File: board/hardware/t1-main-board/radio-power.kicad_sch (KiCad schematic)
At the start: 25 parts, among them U5101 SN74AXC1T45DCKR, U5102 TPS22919DCKR, U5103 TPS62826DMQR

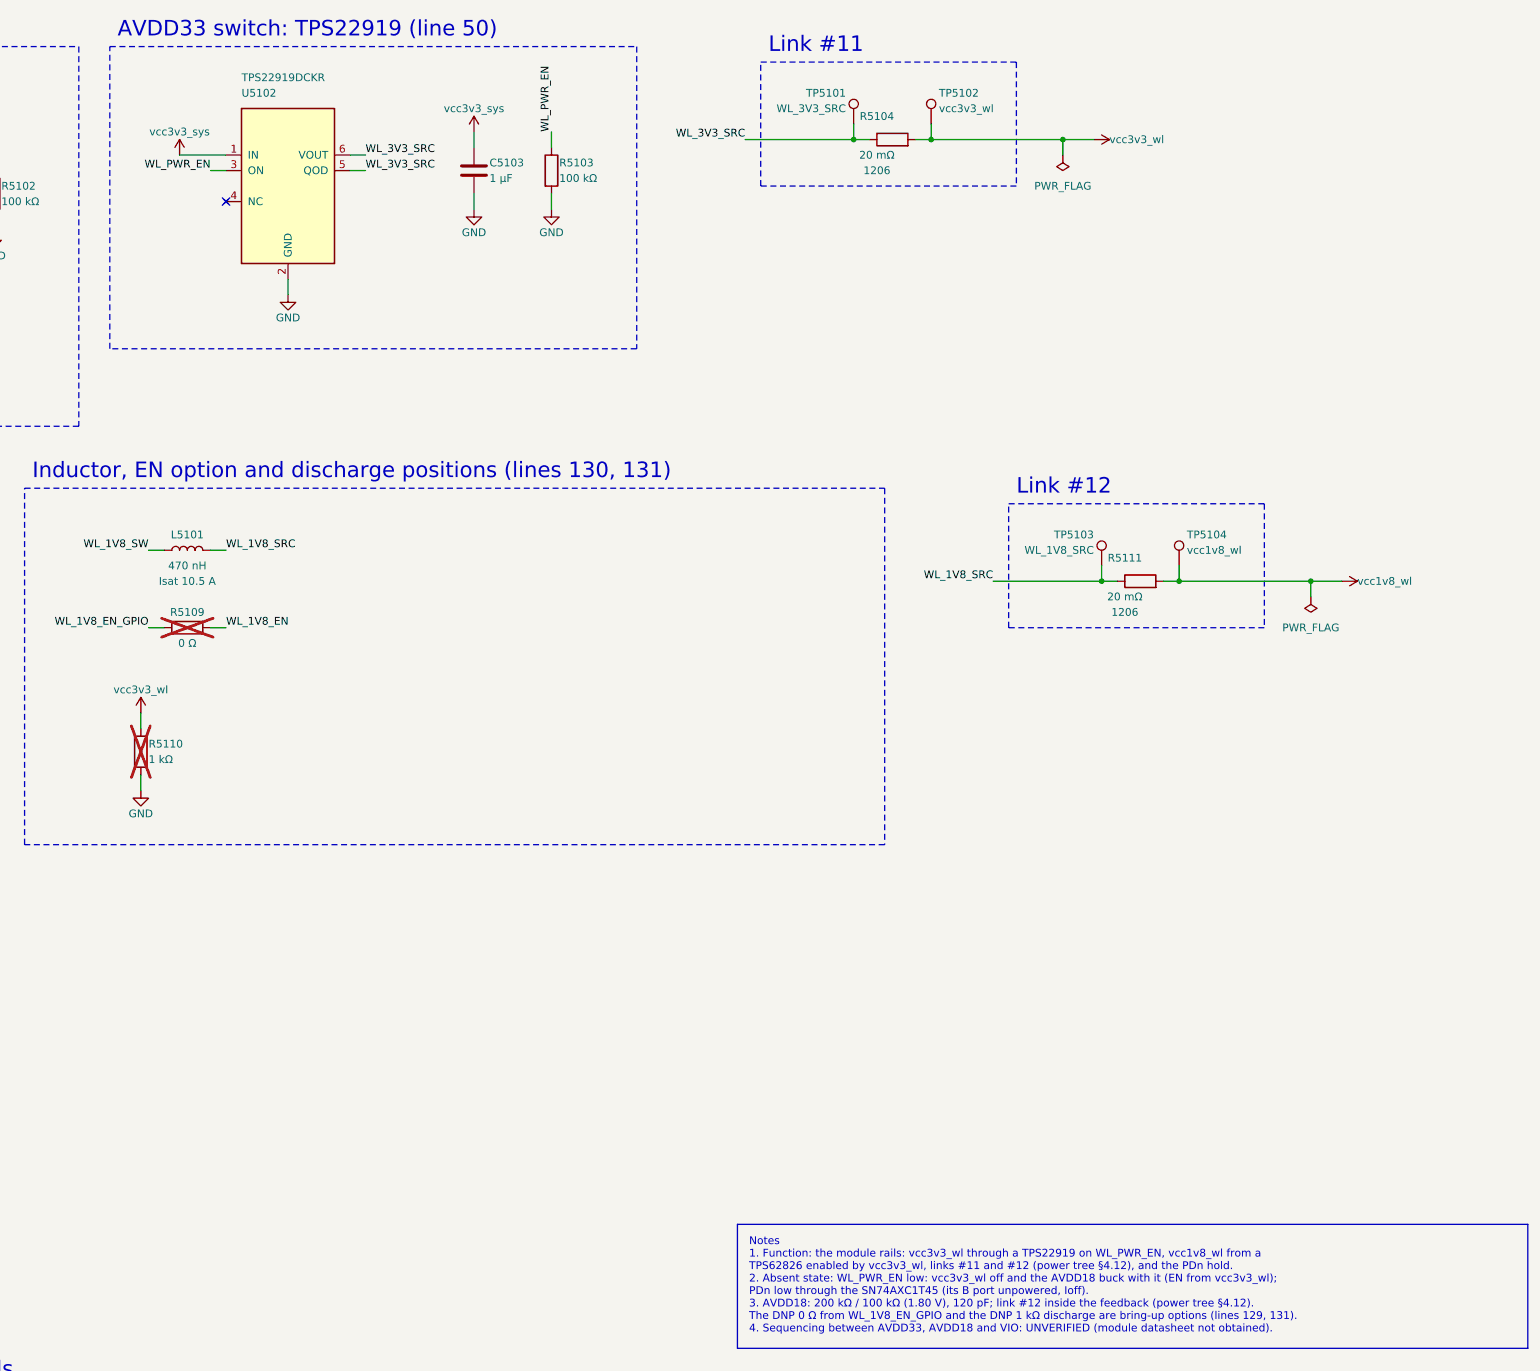
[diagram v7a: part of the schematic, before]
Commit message: Load switches in TPS22916C WCSP (BOM v1.17 item 3, libs v0.3.1)
The six TPS22919DCKR become the TPS22916CYFPR, the BOM's named second
source, now that kicad-lib v0.3.1 carries its land, symbol and model.
Each position's rise time and output discharge checked against the
data sheet (SLVSDO5F section 6.6): every sequencing rule holds; the
fixed 150 Ohm discharge is slower and the driver's delays follow it.
Power tree v0.9 restates the switch rows.

Co-Authored-By: Claude Opus 5.5 <noreply@anthropic.com>
Claude-Session: https://claude.ai/code/session_01Ei262h3TpgY9vyfNLMi5Mn
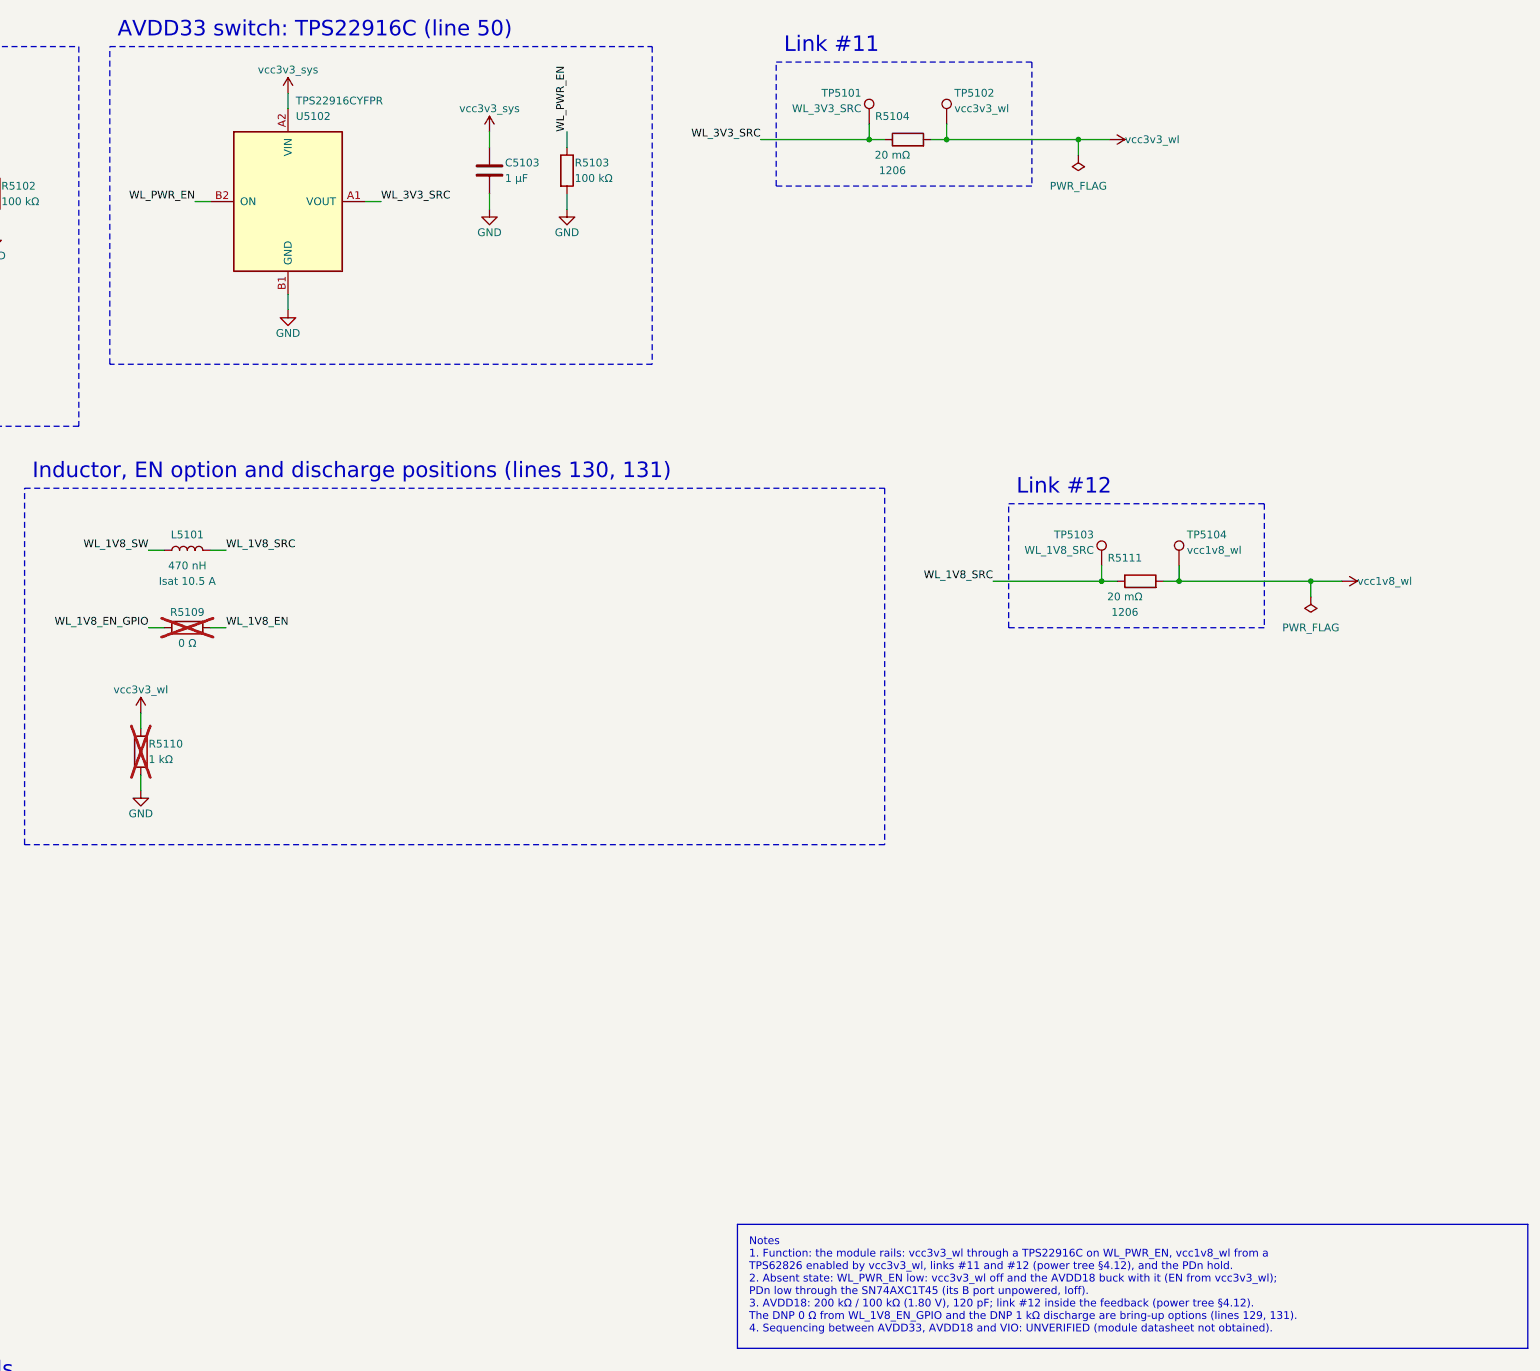
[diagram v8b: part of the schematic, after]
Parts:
- U5102: value TPS22919DCKR -> TPS22916CYFPR; footprint texas-instruments:Texas_DCK0006A_SC-70-6_1.25x2mm_P0.65mm -> texas-instruments:Texas_YFP0004_DSBGA-4_0.78x0.78mm_Layout2x2_P0.4mm; symbol texas-instruments:TPS22919DCKR -> texas-instruments:TPS22916CYFPR; MPN TPS22919DCKR -> TPS22916CYFPR; Second_Source Texas Instruments TPS22916CYFPR (WCSP, other land; BOM v1 l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 -> (none)
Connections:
- net GND: now also U5102.B1 (GND); no longer U5102.2 (GND)
- net WL_3V3_SRC: now also U5102.A1 (VOUT); no longer U5102.5 (QOD), U5102.6 (VOUT)
- net WL_PWR_EN: now also U5102.B2 (ON); no longer U5102.3 (ON)
- net vcc3v3_sys: now also U5102.A2 (VIN); no longer U5102.1 (IN)
- no-connect marks 2 -> 1
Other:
- note added: "AVDD33 switch: TPS22916C (line 50)"
- note removed: "AVDD33 switch: TPS22919 (line 50)"
- moved on the sheet: C5103, R5103, R5104, TP5101, TP5102
